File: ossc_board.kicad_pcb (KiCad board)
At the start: 2 copper layers, 124.6 x 68.7 mm, 230 parts, among them J1 VGA, J2 3XRCA_CONN, J3 SCART-F, J4 HDMI_CONN, J5 5VDC_IN, J6 SJ1-3533NG, J7 SJ1-3533NG, P1 JTAG_CONN, P3 mSD_CONN, Q1 BC847, Q2 BC857, SW1 SPST, SW2 SW_PUSH, SW3 SW_PUSH, SW4 DPDT, U1 TVP7002PZP, U10 S25FL216K, U11 IRM-V538/TR1, U12 TLV70012, U13 TLV70025, U14 TLV70012, U15 TLV70018, U16 TLV70018, U17 THS7353, U2 EP4CE15E22, U3 IT6613, U4 SN74LVC2G17, U5 AP7361C, U6 TLV70033, U7 NCP703SN19T1G, U8 PCM1862, U9 TLV70019, Y1 ACHL-27MHZ-EK, Y2 24.576MHz

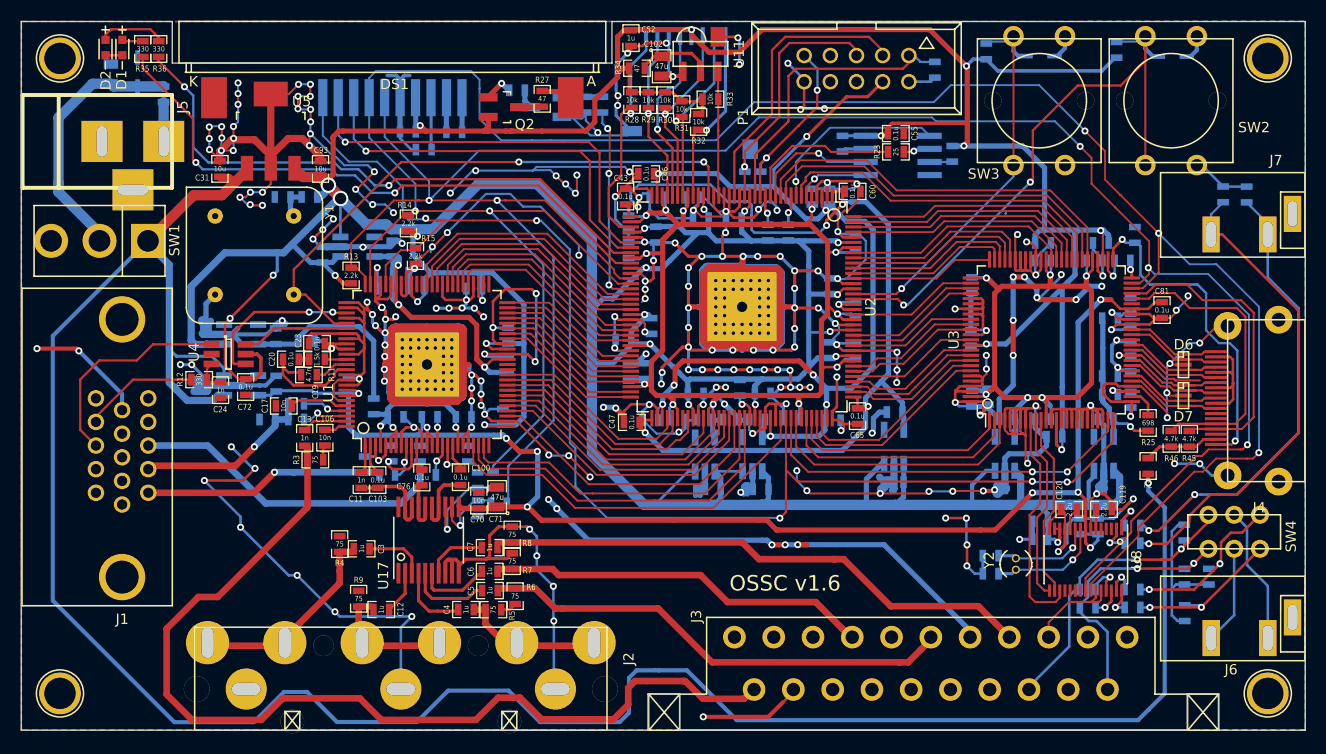
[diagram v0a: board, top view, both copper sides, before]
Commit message: Regenerate PCB files after recent small updates.
- update R12 value on schematic, netlist and layout.
- update ECS-3X9X footprint.
- add pdf of the schematic.
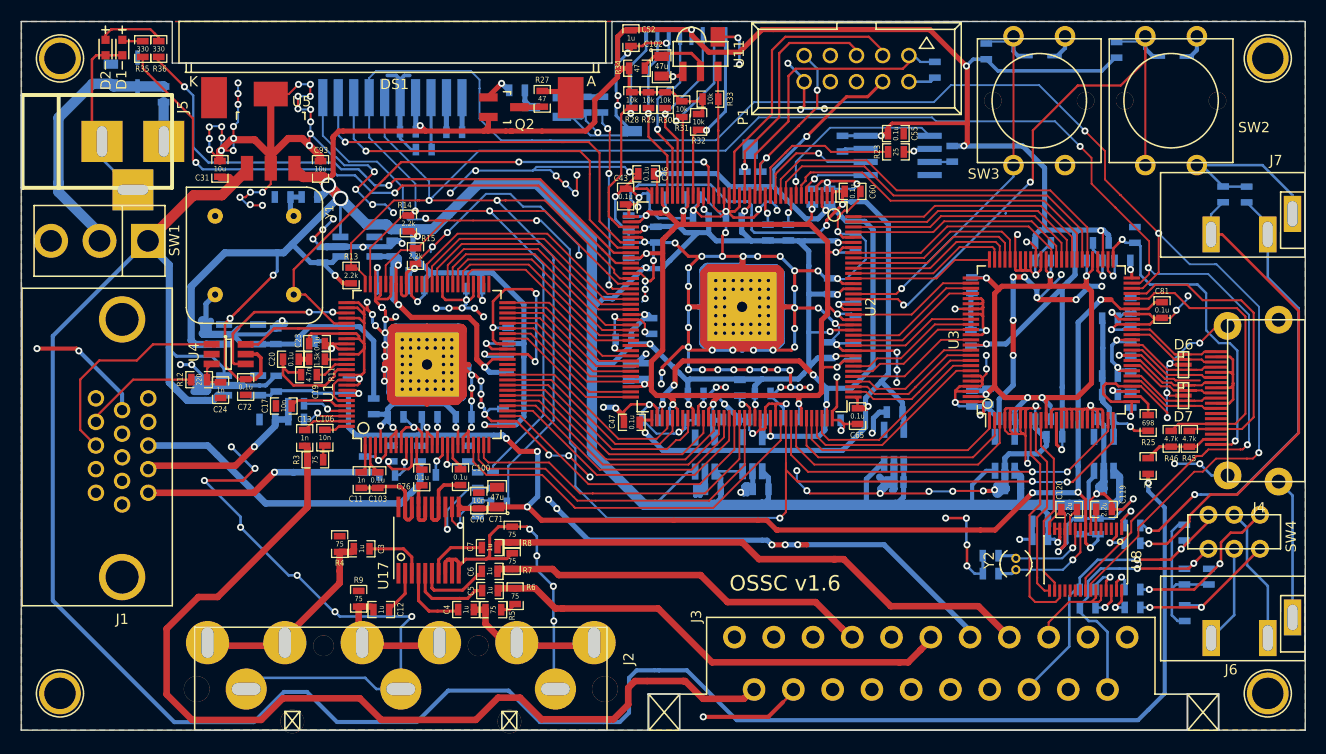
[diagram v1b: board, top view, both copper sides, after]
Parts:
- R12: value 330 -> 220
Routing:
- net GND: track 1327.5 -> 1385.2 mm
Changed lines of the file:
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@@
     (area 7.070879 14.225 132.221001 86.31072)
     (thickness 1.6)
-    (drawings 17)
-    (tracks 4131)
+    (drawings 35)
+    (tracks 4146)
     (zones 0)
     (modules 230)
@@
       (effects (font (size 0.5842 0.508) (thickness 0.127)))
     )
-    (fp_text value 330 (at 0 0 270) (layer F.SilkS)
+    (fp_text value 220 (at 0 0 270) (layer F.SilkS)
       (effects (font (size 0.508 0.4572) (thickness 0.1143)))
     )
@@
     (at 101.42 70.58 180)
     (attr smd)
-    (fp_text reference C111 (at -1.85 -0.22 450) (layer B.SilkS)
+    (fp_text reference C111 (at 1.77 -0.43 450) (layer B.SilkS)
       (effects (font (size 0.5842 0.508) (thickness 0.127)) (justify mirror))
     )
@@
     (at 101.41 68.84 180)
     (attr smd)
-    (fp_text reference C112 (at -1.81 0.31 450) (layer B.SilkS)
+    (fp_text reference C112 (at 1.77 0.2 450) (layer B.SilkS)
       (effects (font (size 0.5842 0.508) (thickness 0.127)) (justify mirror))
     )
@@
     )
   )
-  (module custom_components:ECS-3X9X (layer F.Cu)
-    (at 103.861 69.647 90)
-    (descr "Crystal, Quarz, Rundgehaeuse, round, vertical, stehend, Uhrenquarz, Diam. 3mm,")
-    (tags "Crystal Quarz Rundgehaeuse round vertical stehend Uhrenquarz Diam. 3mm")
-    (fp_text reference Y2 (at 0.36576 -2.59842 90) (layer F.SilkS)
-      (effects (font (size 1 1) (thickness 0.15)))
-    )
-    (fp_text value 24.576MHz (at 0.2413 2.5146 90) (layer F.Fab)
-      (effects (font (size 1 1) (thickness 0.15)))
-    )
-    (fp_line (start 1.30048 0.89916) (end 1.04902 1.15062) (layer F.SilkS) (width 0.15))
-    (fp_line (start 1.04902 1.15062) (end 0.70104 1.39954) (layer F.SilkS) (width 0.15))
-    (fp_line (start 0.70104 1.39954) (end 0.14986 1.5494) (layer F.SilkS) (width 0.15))
-    (fp_line (start 0.14986 1.5494) (end -0.24892 1.5494) (layer F.SilkS) (width 0.15))
-    (fp_line (start -0.24892 1.5494) (end -0.7493 1.34874) (layer F.SilkS) (width 0.15))
-    (fp_line (start -0.7493 1.34874) (end -1.15062 1.00076) (layer F.SilkS) (width 0.15))
-    (fp_line (start 1.30048 -0.8509) (end 1.15062 -1.04902) (layer F.SilkS) (width 0.15))
-    (fp_line (start 1.15062 -1.04902) (end 0.8509 -1.30048) (layer F.SilkS) (width 0.15))
-    (fp_line (start 0.8509 -1.30048) (end 0.39878 -1.50114) (layer F.SilkS) (width 0.15))
-    (fp_line (start 0.39878 -1.50114) (end -0.0508 -1.5494) (layer F.SilkS) (width 0.15))
-    (fp_line (start -0.0508 -1.5494) (end -0.55118 -1.45034) (layer F.SilkS) (width 0.15))
-    (fp_line (start -0.55118 -1.45034) (end -0.89916 -1.24968) (layer F.SilkS) (width 0.15))
-    (fp_line (start -0.89916 -1.24968) (end -1.24968 -0.89916) (layer F.SilkS) (width 0.15))
-    (pad 1 thru_hole circle (at -0.55 0 90) (size 0.8 0.8) (drill 0.5) (layers *.Cu *.Mask F.SilkS)
-      (net 208 "Net-(C111-Pad1)"))
-    (pad 2 thru_hole circle (at 0.55 0 90) (size 0.8 0.8) (drill 0.5) (layers *.Cu *.Mask F.SilkS)
-      (net 209 "Net-(C112-Pad1)"))
-  )
   (module custom_components:SLP2510P8 (layer F.Cu)
     (at 120.12 53.31 270)
@@
       (net 107 GND))
   )
+  (module custom_components:ECS-3X9X (layer F.Cu)
+    (at 103.861 69.647 90)
+    (descr "Crystal, Quarz, Rundgehaeuse, round, vertical, stehend, Uhrenquarz, Diam. 3mm,")
+    (tags "Crystal Quarz Rundgehaeuse round vertical stehend Uhrenquarz Diam. 3mm")
+    (fp_text reference Y2 (at 0.36576 -2.59842 90) (layer F.SilkS)
+      (effects (font (size 1 1) (thickness 0.15)))
+    )
+    (fp_text value 24.576MHz (at 0.2413 2.5146 90) (layer F.Fab)
+      (effects (font (size 1 1) (thickness 0.15)))
+    )
+    (fp_line (start 1.30048 0.89916) (end 1.04902 1.15062) (layer F.SilkS) (width 0.15))
+    (fp_line (start 1.04902 1.15062) (end 0.70104 1.39954) (layer F.SilkS) (width 0.15))
+    (fp_line (start 0.70104 1.39954) (end 0.14986 1.5494) (layer F.SilkS) (width 0.15))
+    (fp_line (start 0.14986 1.5494) (end -0.24892 1.5494) (layer F.SilkS) (width 0.15))
+    (fp_line (start -0.24892 1.5494) (end -0.7493 1.34874) (layer F.SilkS) (width 0.15))
+    (fp_line (start -0.7493 1.34874) (end -1.15062 1.00076) (layer F.SilkS) (width 0.15))
+    (fp_line (start 1.30048 -0.8509) (end 1.15062 -1.04902) (layer F.SilkS) (width 0.15))
+    (fp_line (start 1.15062 -1.04902) (end 0.8509 -1.30048) (layer F.SilkS) (width 0.15))
+    (fp_line (start 0.8509 -1.30048) (end 0.39878 -1.50114) (layer F.SilkS) (width 0.15))
+    (fp_line (start 0.39878 -1.50114) (end -0.0508 -1.5494) (layer F.SilkS) (width 0.15))
+    (fp_line (start -0.0508 -1.5494) (end -0.55118 -1.45034) (layer F.SilkS) (width 0.15))
+    (fp_line (start -0.55118 -1.45034) (end -0.89916 -1.24968) (layer F.SilkS) (width 0.15))
+    (fp_line (start -0.89916 -1.24968) (end -1.24968 -0.89916) (layer F.SilkS) (width 0.15))
+    (pad 1 thru_hole circle (at -0.55 0 90) (size 0.9 0.9) (drill 0.5) (layers *.Cu *.Mask F.SilkS)
+      (net 208 "Net-(C111-Pad1)"))
+    (pad 2 thru_hole circle (at 0.55 0 90) (size 0.9 0.9) (drill 0.5) (layers *.Cu *.Mask F.SilkS)
+      (net 209 "Net-(C112-Pad1)"))
+  )
   (gr_line (start 58.386 81.7762) (end 60.006 81.7762) (layer Edge.Cuts) (width 1.2))
   (gr_line (start 62.946 76.376) (end 62.946 78.176) (layer Edge.Cuts) (width 1.2))
@@
   (segment (start 51.7398 59.5398) (end 51.7398 58.039) (width 0.18) (layer F.Cu) (net 106))
   (segment (start 61.3156 63.5) (end 60.9588 63.1432) (width 0.18) (layer F.Cu) (net 106))
+  (segment (start 44.196 81.7762) (end 41.8262 81.7762) (width 0.25) (layer B.Cu) (net 107))
+  (segment (start 40.74 80.69) (end 30.2822 80.69) (width 0.25) (layer B.Cu) (net 107))
+  (segment (start 41.8262 81.7762) (end 40.74 80.69) (width 0.25) (layer B.Cu) (net 107))
+  (segment (start 30.2822 80.69) (end 29.196 81.7762) (width 0.25) (layer B.Cu) (net 107))
+  (segment (start 15.549 20.2943) (end 14.6457 20.2943) (width 0.25) (layer F.Cu) (net 107))
+  (segment (start 14.23 20.71) (end 14.23 27.67634) (width 0.25) (layer F.Cu) (net 107))
+  (segment (start 14.6457 20.2943) (end 14.23 20.71) (width 0.25) (layer F.Cu) (net 107))
+  (segment (start 14.23 27.67634) (end 15.20266 28.649) (width 0.25) (layer F.Cu) (net 107))
+  (segment (start 15.20266 28.649) (end 15.20266 30.34826) (width 0.25) (layer B.Cu) (net 107))
+  (segment (start 15.20266 30.34826) (end 18.2024 33.348) (width 0.25) (layer B.Cu) (net 107))
+  (segment (start 121.418 30.95) (end 127.78 30.95) (width 0.25) (layer B.Cu) (net 107))
+  (segment (start 130.698 33.868) (end 130.698 35.676) (width 0.25) (layer B.Cu) (net 107))
+  (segment (start 127.78 30.95) (end 130.698 33.868) (width 0.25) (layer B.Cu) (net 107))
+  (segment (start 130.706 74.83) (end 130.706 63.006) (width 0.25) (layer B.Cu) (net 107))
+  (segment (start 130.706 63.006) (end 129.35 61.65) (width 0.25) (layer B.Cu) (net 107))
   (segment (start 100.658 70.58) (end 99.86 70.58) (width 0.25) (layer B.Cu) (net 107))
   (via (at 97.05 65.19) (size 0.686) (drill 0.35) (layers F.Cu B.Cu) (net 107))

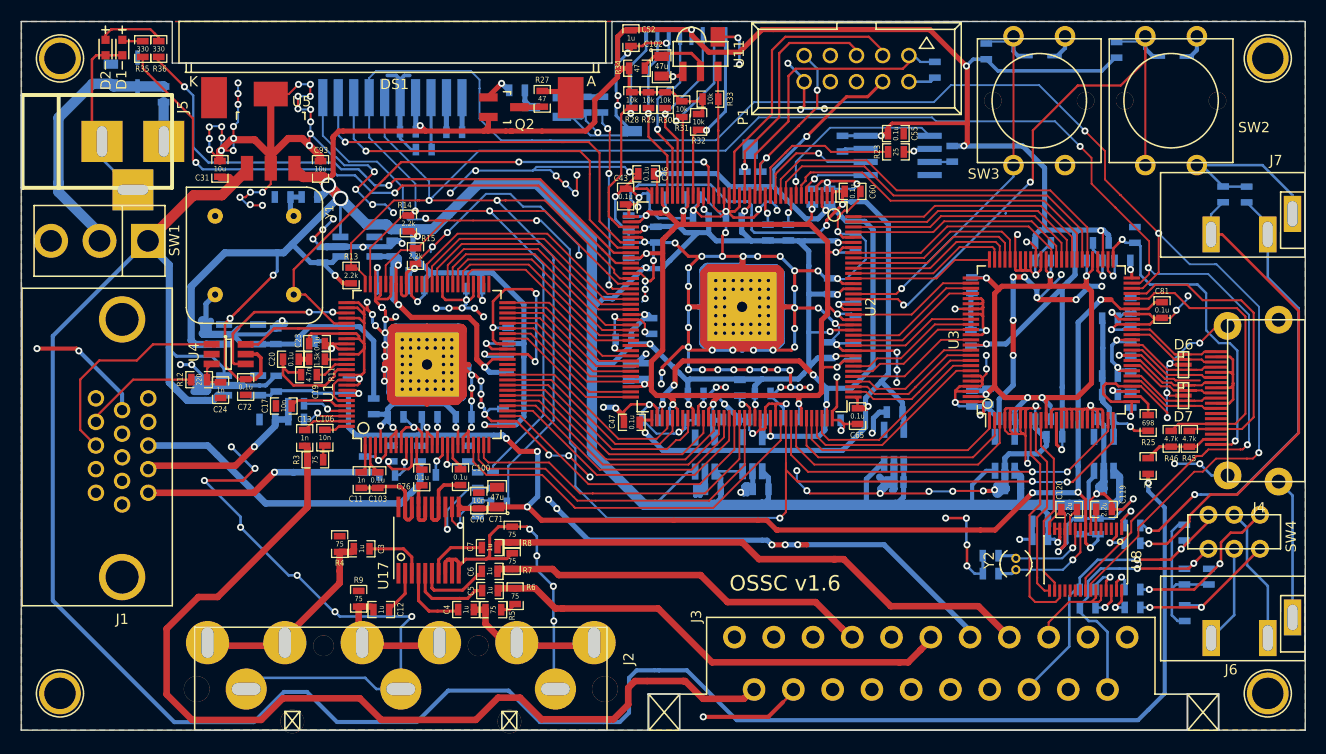
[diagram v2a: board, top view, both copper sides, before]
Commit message: update to Kicad 5.x symbols
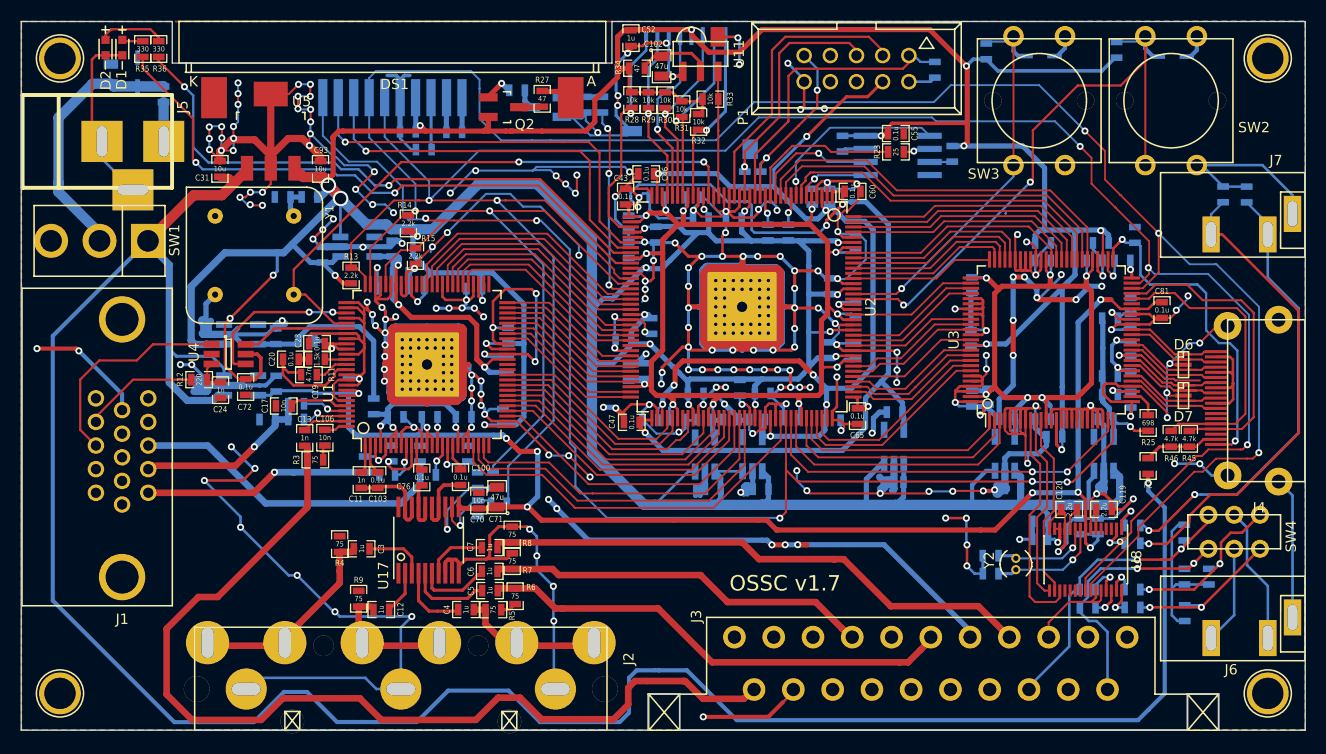
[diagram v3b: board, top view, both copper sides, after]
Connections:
- D1 pad 1: Net-(D1-Pad1) -> GND
- D1 pad 2: GND -> Net-(D1-Pad2)
- D2 pad 1: Net-(D2-Pad1) -> GND
- D2 pad 2: GND -> Net-(D2-Pad2)
- MH1 pad 1: Net-(MH1-Pad1) -> (no net)
- MH2 pad 1: Net-(MH2-Pad1) -> (no net)
- MH3 pad 1: Net-(MH3-Pad1) -> (no net)
- MH4 pad 1: Net-(MH4-Pad1) -> (no net)
- R35 pad 1: Net-(D1-Pad1) -> Net-(D1-Pad2)
- R36 pad 1: Net-(D2-Pad1) -> Net-(D2-Pad2)
- U12 pad 4: (no net) -> Net-(U12-Pad4)
- U13 pad 4: (no net) -> Net-(U13-Pad4)
- U14 pad 4: (no net) -> Net-(U14-Pad4)
- U15 pad 4: (no net) -> Net-(U15-Pad4)
- U16 pad 4: (no net) -> Net-(U16-Pad4)
- U6 pad 4: (no net) -> Net-(U6-Pad4)
- U7 pad 4: (no net) -> Net-(U7-Pad4)
- U9 pad 4: (no net) -> Net-(U9-Pad4)
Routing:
- net Net-(D2-Pad2): track 0.00 -> 6.60 mm
- net Net-(D2-Pad1): track 6.60 -> 0.00 mm
- net Net-(D1-Pad2): track 0.00 -> 2.04 mm
- net Net-(D1-Pad1): track 2.04 -> 0.00 mm
- net GND: vias 240 -> 239
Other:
- board text added: "OSSC v1.7"
- board text removed: "OSSC v1.6"

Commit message: update to pcb v1.7
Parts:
- added C117: 10u, custom_components:SM0603_Capa_libcms, B.Cu at (23.4, 39.0)
- added C122: 10u, custom_components:SM0603_Capa_libcms, B.Cu at (34.9, 41.2)
- added C127: 10n, custom_components:SM0603_Capa_libcms, B.Cu at (114.0, 65.5)
- added C128: 10n, custom_components:SM0603_Capa_libcms, B.Cu at (114.0, 67.2)
- added C129: 10n, custom_components:SM0603_Capa_libcms, B.Cu at (114.9, 73.1)
- added C130: 10n, custom_components:SM0603_Capa_libcms, B.Cu at (107.8, 74.1)
- added C131: 10n, custom_components:SM0603_Capa_libcms, B.Cu at (114.9, 71.4)
- added C132: 10n, custom_components:SM0603_Capa_libcms, B.Cu at (112.7, 71.9)
- added D10: PESD5V0U4BW, Package_TO_SOT_SMD:SOT-665, B.Cu at (49.0, 81.7)
- added D11: PESD12VL2BT, Package_TO_SOT_SMD:SOT-23_Handsoldering, B.Cu at (125.5, 73.7)
- added D12: PESD12VL2BT, Package_TO_SOT_SMD:SOT-23_Handsoldering, B.Cu at (125.6, 34.6)
- added D13: PESD5V0V4UW, Package_TO_SOT_SMD:SOT-665, B.Cu at (19.1, 50.8)
- added D14: BZX84C5V1/SOT, Package_TO_SOT_SMD:SOT-23_Handsoldering, B.Cu at (19.2, 18.9)
- added D15: PESD5V0V4UW, Package_TO_SOT_SMD:SOT-665, B.Cu at (120.0, 57.4)
- added D8: PESD5V0U4BW, Package_TO_SOT_SMD:SOT-665, B.Cu at (72.7, 73.8)
- added D9: PESD5V0U4BW, Package_TO_SOT_SMD:SOT-665, B.Cu at (22.8, 61.5)
- added L1: 2.2u, custom_components:CDRH2D14, B.Cu at (31.9, 39.3)
- added Q3: AOSS21115C, Package_TO_SOT_SMD:SOT-23_Handsoldering, B.Cu at (21.0, 22.9)
- added Q4: DSS20200L, Package_TO_SOT_SMD:SOT-23_Handsoldering, B.Cu at (10.1, 27.1)
- added Q5: AOSS21115C, Package_TO_SOT_SMD:SOT-23_Handsoldering, B.Cu at (12.7, 33.4)
- added R53: 27k, custom_components:SM0603_Resistor_libcms, B.Cu at (18.6, 25.4)
- added R54: 27k, custom_components:SM0603_Resistor_libcms, B.Cu at (16.3, 24.2)
- added R55: 330, custom_components:SM0805_libcms, B.Cu at (16.6, 21.6)
- added R56: 6.8k, custom_components:SM0603_Resistor_libcms, B.Cu at (15.8, 19.0)
- added R57: 100k, custom_components:SM0603_Resistor_libcms, B.Cu at (9.77, 30.9)
- added R58: 6.8k, custom_components:SM0603_Resistor_libcms, B.Cu at (8.82, 34.1)
- added R59: 100, custom_components:SM0603_Resistor_libcms, B.Cu at (116.9, 61.8)
- added R60: 100, custom_components:SM0603_Resistor_libcms, B.Cu at (116.9, 63.5)
- added R61: 100, custom_components:SM0603_Resistor_libcms, B.Cu at (117.1, 73.6)
- added R62: 100, custom_components:SM0603_Resistor_libcms, B.Cu at (107.8, 72.4)
- added R63: 100, custom_components:SM0603_Resistor_libcms, B.Cu at (117.1, 70.9)
- added R64: 100, custom_components:SM0603_Resistor_libcms, B.Cu at (112.2, 74.1)
- added U18: LM3671MF-2.5/NOPB, custom_components:SOT-23-5_Handsoldering, B.Cu at (27.0, 39.7)
- D3, D4: value SD05-7 -> PESD3V3V4UW; footprint custom_components:SOD-323_Handsoldering -> Package_TO_SOT_SMD:SOT-665
- D5: value SD05-7 -> PESD12VL2BT; footprint custom_components:SOD-323_Handsoldering -> Package_TO_SOT_SMD:SOT-23_Handsoldering
- F1: value F0603E1R50FSTR -> F0603E1R25FSTR
- Q1, Q2: footprint Housings_SOT-23_SOT-143_TSOT-6:SOT-23_Handsoldering -> Package_TO_SOT_SMD:SOT-23_Handsoldering
- SW4: value DPDT -> GW22RCV; footprint custom_components:MS22 -> custom_components:GW22RxV
- moved D5 114.1 mm to (116.7, 80.3)
- moved D4 25.5 mm to (80.7, 20.8), turned to 180 degrees
- moved C107 20.4 mm to (20.0, 42.1), turned to 180 degrees
- moved R52 20.2 mm to (104.4, 79.3), turned to 180 degrees
- moved D3 18.6 mm to (105.2, 32.8)
- moved R50 14.5 mm to (108.4, 79.3), turned to 0 degrees
- moved SW4 8.20 mm to (116.8, 66.5), turned to 90 degrees
- moved R51 7.91 mm to (124.5, 67.8), turned to 180 degrees
- moved C116 6.07 mm to (119.6, 63.5)
- moved C121 6.06 mm to (119.6, 61.8)
- moved R49 5.94 mm to (124.5, 65.3), turned to 0 degrees
- moved C126 5.38 mm to (105.6, 73.6), turned to 270 degrees
- moved C125 3.85 mm to (118.8, 70.9), turned to 270 degrees
- moved C123 3.64 mm to (118.8, 73.6), turned to 90 degrees
- moved C124 1.99 mm to (111.0, 71.9), turned to 90 degrees
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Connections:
- C107 pad 1: Net-(C107-Pad1) -> /hdmitx1/5V
- C32 pad 2: /hdmitx1/DVDD3V3 -> /tvp_board1/DVDD2V5
- C34 pad 1: /hdmitx1/DVDD3V3 -> /tvp_board1/DVDD2V5
- D4 pad 1: /fpga1/BTN1 -> /fpga1/TDI
- D5 pad 1: Net-(C107-Pad1) -> /hdmitx1/AV1_AUD_L
- D5 pad 2: GND -> /hdmitx1/AV1_AUD_R
- F1 pad 2: Net-(C107-Pad1) -> Net-(F1-Pad2)
- SW1 pad 2: Net-(C107-Pad1) -> Net-(Q5-Pad3)
- SW4 pad 1: /hdmitx1/AV2_AUD_L -> /hdmitx1/AV1_AUD_L
- SW4 pad 3: /hdmitx1/AV1_AUD_L -> /hdmitx1/AV2_AUD_L
- SW4 pad 4: /hdmitx1/AV2_AUD_R -> /hdmitx1/AV1_AUD_R
- SW4 pad 6: /hdmitx1/AV1_AUD_R -> /hdmitx1/AV2_AUD_R
- U7 pad 1: /hdmitx1/DVDD3V3 -> /tvp_board1/DVDD2V5
- U7 pad 3: /hdmitx1/DVDD3V3 -> /tvp_board1/DVDD2V5
- U8 pad 1: Net-(C121-Pad2) -> Net-(C127-Pad2)
- U8 pad 2: Net-(C116-Pad2) -> Net-(C128-Pad1)
- U8 pad 27: Net-(C126-Pad1) -> Net-(C130-Pad1)
- U8 pad 28: Net-(C124-Pad1) -> Net-(C132-Pad2)
- U8 pad 29: Net-(C125-Pad1) -> Net-(C131-Pad1)
- U8 pad 30: Net-(C123-Pad1) -> Net-(C129-Pad2)
- U9 pad 1: /hdmitx1/DVDD3V3 -> /tvp_board1/DVDD2V5
- U9 pad 3: /hdmitx1/DVDD3V3 -> /tvp_board1/DVDD2V5
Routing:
- net /tvp_board1/DVDD2V5: track 0.00 -> 45.2 mm
- net /hdmitx1/DVDD3V3: track 614.8 -> 588.3 mm
- net Net-(C107-Pad1): track 25.3 -> 0.00 mm
- net /hdmitx1/5V: track 229.4 -> 249.7 mm, vias 1 -> 3
- net /tvp_board1/RGB2_R: track 20.3 -> 38.8 mm
- net Net-(Q3-Pad2): track 0.00 -> 18.4 mm
- net Net-(Q4-Pad1): track 0.00 -> 17.3 mm
- net /hdmitx1/AV1_AUD_L: track 29.4 -> 45.8 mm
- net Net-(C128-Pad1): track 0.00 -> 10.2 mm, vias 0 -> 1
- net /tvp_board1/RGB2_B: track 13.9 -> 24.0 mm
- net /tvp_board1/RGB1_S: track 95.9 -> 105.2 mm
- net Net-(C130-Pad1): track 0.00 -> 8.36 mm, vias 0 -> 1
- net Net-(Q4-Pad3): track 0.00 -> 8.28 mm
- net Net-(C127-Pad2): track 0.00 -> 8.07 mm, vias 0 -> 1
- net /tvp_board1/RGB1_B: track 53.8 -> 61.6 mm, vias 0 -> 1
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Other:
- net class 75ohm_vid: clearance 0.24 -> 0.2
